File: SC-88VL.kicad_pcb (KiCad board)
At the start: 2 copper layers, 77.5 x 64.8 mm, 13 parts

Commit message: The initial design was missing a via.
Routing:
- net (no net): track 931.8 -> 931.1 mm, vias 24 -> 25

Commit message: Removed a useless via
Removed a useless via
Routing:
- net (no net): vias 25 -> 24
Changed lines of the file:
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@@
     (thickness 1.6)
     (drawings 4)
-    (tracks 176)
+    (tracks 175)
     (zones 0)
     (modules 13)
@@
   (segment (start 97.79 41.91) (end 101.6 45.72) (width 0.25) (layer B.Cu) (net 0))
   (segment (start 101.6 45.72) (end 101.6 45.72) (width 0.25) (layer B.Cu) (net 0))
-  (via (at 101.6 45.72) (size 0.8) (drill 0.4) (layers F.Cu B.Cu) (net 0))
-  (via (at 101.6 48.26) (size 0.8) (drill 0.4) (layers F.Cu B.Cu) (net 0))
+  (via (at 101.6 45.72) (size 0.8) (drill 0.4) (layers F.Cu B.Cu) (net 0) (status 1000000))
   (segment (start 101.6 45.72) (end 101.6 48.26) (width 0.25) (layer F.Cu) (net 0))
   (segment (start 102.87 59.69) (end 102.87 59.69) (width 0.25) (layer B.Cu) (net 0))

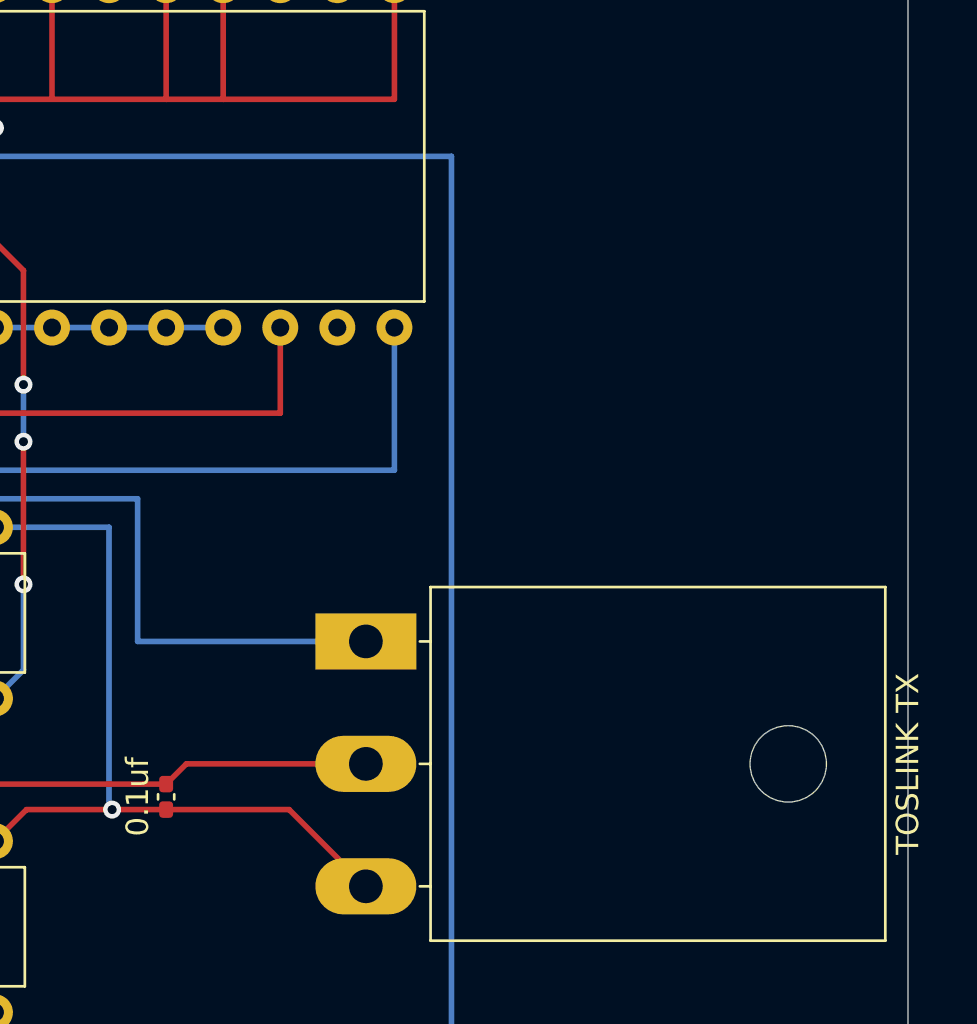
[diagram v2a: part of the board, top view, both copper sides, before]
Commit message: Added an optional TOTX170 footprint
Added an optional TOTX170 footprint, use either this one or the regular TOSLINK footprint (not both at the same time)
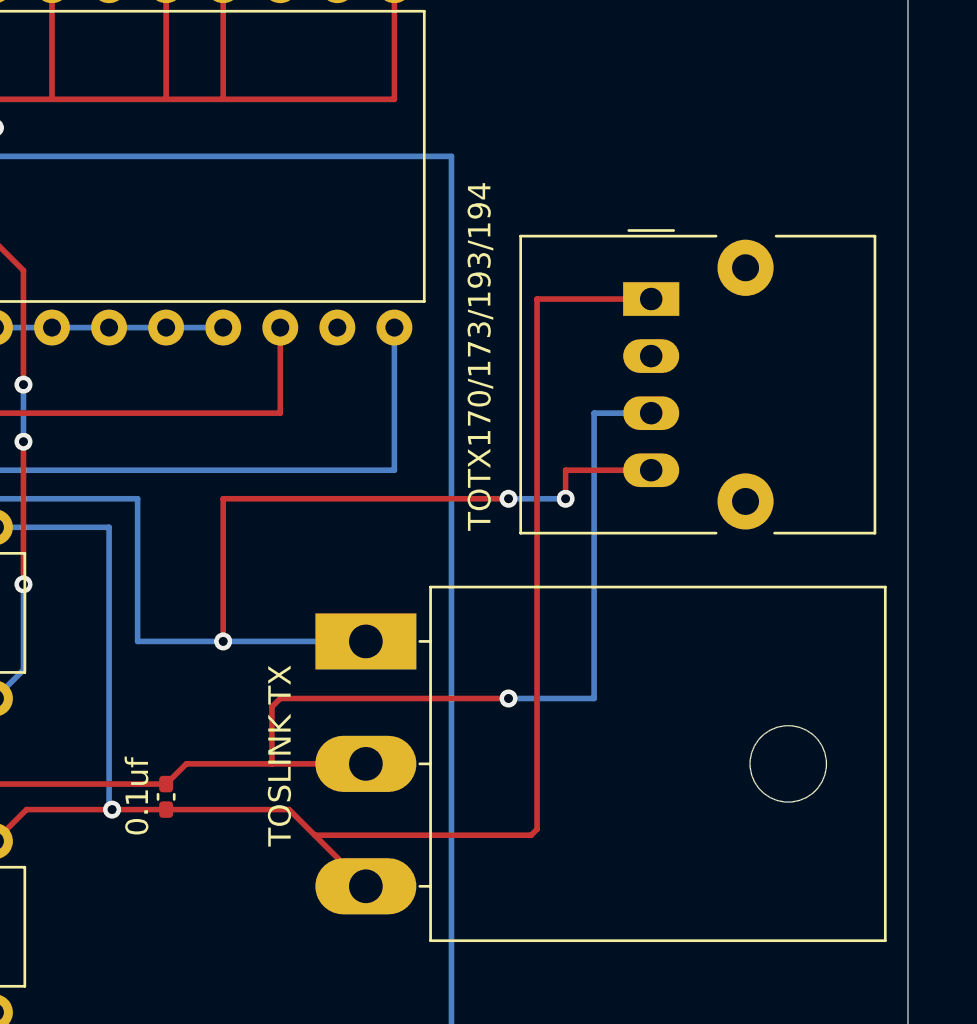
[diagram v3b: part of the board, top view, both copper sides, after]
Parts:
- added TOTX170/173/193/194: Toshiba_TOTX170_TOTX173_TOTX193_TOTX194, OptoDevice:Toshiba_TOTX170_TOTX173_TOTX193_TOTX194, F.Cu at (130.8, 53.3)
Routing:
- net (no net): track 931.1 -> 1028.7 mm, vias 24 -> 28
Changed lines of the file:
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@@
     (thickness 1.6)
     (drawings 4)
-    (tracks 175)
+    (tracks 199)
     (zones 0)
-    (modules 13)
+    (modules 14)
     (nets 1)
   )
@@
     (uvia_drill 0.1)
   )
+  (module OptoDevice:Toshiba_TOTX170_TOTX173_TOTX193_TOTX194 (layer F.Cu)
+    (at 130.81 53.34 270)
+    (descr "Fiberoptic Reciver, RX, Toshiba, Toslink, TORX170, TORX173, TORX193, TORX194")
+    (tags "Fiberoptic Reciver RX Toshiba Toslink TORX170 TORX173 TORX193 TORX194")
+    (fp_text reference TOTX170/173/193/194 (at 2.54 7.62 90) (layer F.SilkS)
+      (effects (font (size 1 1) (thickness 0.15)))
+    )
+    (fp_text value Toshiba_TOTX170_TOTX173_TOTX193_TOTX194 (at 3.81 7 90) (layer F.Fab)
+      (effects (font (size 1 1) (thickness 0.15)))
+    )
+    (fp_line (start -3.05 1) (end -3.05 -1) (layer F.SilkS) (width 0.12))
+    (fp_line (start -1.69 0) (end -2.69 -1) (layer F.Fab) (width 0.1))
+    (fp_line (start -1.69 0) (end -2.69 1) (layer F.Fab) (width 0.1))
+    (fp_line (start -2.69 -1) (end -2.69 -9.85) (layer F.Fab) (width 0.1))
+    (fp_line (start 10.56 5.95) (end -2.94 5.95) (layer F.CrtYd) (width 0.05))
+    (fp_line (start 10.56 5.95) (end 10.56 -10.1) (layer F.CrtYd) (width 0.05))
+    (fp_line (start -2.94 -10.1) (end -2.94 5.95) (layer F.CrtYd) (width 0.05))
+    (fp_line (start -2.94 -10.1) (end 10.56 -10.1) (layer F.CrtYd) (width 0.05))
+    (fp_line (start -2.8 5.81) (end 10.42 5.81) (layer F.SilkS) (width 0.12))
+    (fp_line (start 10.42 -9.96) (end -2.8 -9.96) (layer F.SilkS) (width 0.12))
+    (fp_line (start 1.81 -8.1) (end 1.81 -9.1) (layer F.Fab) (width 0.1))
+    (fp_line (start 5.81 -8.1) (end 1.81 -8.1) (layer F.Fab) (width 0.1))
+    (fp_line (start 5.81 -9.1) (end 5.81 -8.1) (layer F.Fab) (width 0.1))
+    (fp_line (start 1.81 -9.1) (end 5.81 -9.1) (layer F.Fab) (width 0.1))
+    (fp_line (start 10.42 -9.96) (end 10.42 -5.49) (layer F.SilkS) (width 0.12))
+    (fp_line (start 10.42 5.81) (end 10.42 -2.89) (layer F.SilkS) (width 0.12))
+    (fp_line (start -2.8 -9.96) (end -2.8 -5.56) (layer F.SilkS) (width 0.12))
+    (fp_line (start -2.8 5.81) (end -2.8 -2.89) (layer F.SilkS) (width 0.12))
+    (fp_line (start -2.69 5.65) (end -2.69 1) (layer F.Fab) (width 0.1))
+    (fp_line (start -2.69 -9.85) (end 10.31 -9.85) (layer F.Fab) (width 0.1))
+    (fp_line (start 10.31 5.7) (end 10.31 -9.85) (layer F.Fab) (width 0.1))
+    (fp_line (start 10.26 5.7) (end 10.31 5.7) (layer F.Fab) (width 0.1))
+    (fp_line (start -2.69 5.7) (end 10.26 5.7) (layer F.Fab) (width 0.1))
+    (fp_line (start -2.69 5.65) (end -2.69 5.7) (layer F.Fab) (width 0.1))
+    (fp_text user %R (at 3.81 -2.075 90) (layer F.Fab)
+      (effects (font (size 1 1) (thickness 0.15)))
+    )
+    (pad 1 thru_hole rect (at 0 0 270) (size 1.5 2.5) (drill 1) (layers *.Cu *.Mask))
+    (pad 2 thru_hole oval (at 2.54 0 270) (size 1.5 2.5) (drill 1) (layers *.Cu *.Mask))
+    (pad 3 thru_hole oval (at 5.08 0 270) (size 1.5 2.5) (drill 1) (layers *.Cu *.Mask))
+    (pad 4 thru_hole oval (at 7.62 0 270) (size 1.5 2.5) (drill 1) (layers *.Cu *.Mask))
+    (pad 5 thru_hole circle (at 9.01 -4.2 270) (size 2.5 2.5) (drill 1.2) (layers *.Cu *.Mask))
+    (pad 6 thru_hole circle (at -1.39 -4.2 270) (size 2.5 2.5) (drill 1.2) (layers *.Cu *.Mask))
+    (model ${KISYS3DMOD}/OptoDevice.3dshapes/Toshiba_TOTX170_TOTX173_TOTX193_TOTX194.wrl
+      (at (xyz 0 0 0))
+      (scale (xyz 1 1 1))
+      (rotate (xyz 0 0 0))
+    )
+  )
   (module Package_DIP:DIP-28_W15.24mm (layer F.Cu)
     (at 86.36 54.61 90)
@@
     (descr "TO-3P-3, Horizontal, RM 5.45mm, , see https://toshiba.semicon-storage.com/ap-en/design-support/package/detail.TO-3P(N).html")
     (tags "TO-3P-3 Horizontal RM 5.45mm ")
-    (fp_text reference "TOSLINK TX" (at 5.45 -24.12 90) (layer F.SilkS)
+    (fp_text reference "TOSLINK TX" (at 5.08 3.81 90) (layer F.SilkS)
       (effects (font (size 1 1) (thickness 0.15)))
     )
@@
     (fp_line (start -2.3 -18.8) (end -2.3 -21) (layer F.Fab) (width 0.1))
     (fp_circle (center 5.45 -18.8) (end 7.05 -18.8) (layer F.Fab) (width 0.1))
-    (fp_text user %R (at 5.45 -24.12 90) (layer F.Fab)
+    (fp_text user %R (at 5.08 3.81 90) (layer F.Fab)
       (effects (font (size 1 1) (thickness 0.15)))
     )
@@
     )
   )
+  (gr_line (start 142.24 33.02) (end 142.24 97.79) (layer Edge.Cuts) (width 0.05))
   (gr_line (start 64.77 97.79) (end 64.77 33.02) (layer Edge.Cuts) (width 0.05))
   (gr_line (start 142.24 97.79) (end 64.77 97.79) (layer Edge.Cuts) (width 0.05))
-  (gr_line (start 142.24 33.02) (end 142.24 97.79) (layer Edge.Cuts) (width 0.05))
   (gr_line (start 64.77 33.02) (end 142.24 33.02) (layer Edge.Cuts) (width 0.05))
   (segment (start 67.31 43.18) (end 67.31 35.56) (width 0.25) (layer F.Cu) (net 0))
@@
   (segment (start 78.74 62.23) (end 78.74 52.07) (width 0.25) (layer F.Cu) (net 0))
   (segment (start 78.74 52.07) (end 73.66 52.07) (width 0.25) (layer F.Cu) (net 0))
-  (segment (start 114.695 76.065) (end 118.11 79.48) (width 0.25) (layer F.Cu) (net 0))
   (segment (start 109.22 76.065) (end 114.695 76.065) (width 0.25) (layer F.Cu) (net 0))
   (segment (start 110.12 74.03) (end 109.22 74.93) (width 0.25) (layer F.Cu) (net 0))
-  (segment (start 118.11 74.03) (end 110.12 74.03) (width 0.25) (layer F.Cu) (net 0))
   (segment (start 106.815 76.065) (end 103.005 76.065) (width 0.25) (layer F.Cu) (net 0))
   (via (at 106.815 76.065) (size 0.8) (drill 0.4) (layers F.Cu B.Cu) (net 0))
@@
   (segment (start 106.68 75.93) (end 106.815 76.065) (width 0.25) (layer B.Cu) (net 0))
   (segment (start 106.68 63.5) (end 106.68 75.93) (width 0.25) (layer B.Cu) (net 0))
-  (segment (start 118.11 68.58) (end 107.95 68.58) (width 0.25) (layer B.Cu) (net 0))
+  (segment (start 118.11 68.58) (end 111.76 68.58) (width 0.25) (layer B.Cu) (net 0))
   (segment (start 107.95 68.58) (end 107.95 62.23) (width 0.25) (layer B.Cu) (net 0))
   (segment (start 107.95 62.23) (end 99.06 62.23) (width 0.25) (layer B.Cu) (net 0))
@@
   (segment (start 97.79 41.91) (end 101.6 45.72) (width 0.25) (layer B.Cu) (net 0))
   (segment (start 101.6 45.72) (end 101.6 45.72) (width 0.25) (layer B.Cu) (net 0))
-  (via (at 101.6 45.72) (size 0.8) (drill 0.4) (layers F.Cu B.Cu) (net 0) (status 1000000))
+  (via (at 101.6 45.72) (size 0.8) (drill 0.4) (layers F.Cu B.Cu) (net 0))
   (segment (start 101.6 45.72) (end 101.6 48.26) (width 0.25) (layer F.Cu) (net 0))
   (segment (start 102.87 59.69) (end 102.87 59.69) (width 0.25) (layer B.Cu) (net 0))
@@
   (via (at 102.87 57.15) (size 0.8) (drill 0.4) (layers F.Cu B.Cu) (net 0))
   (segment (start 102.87 57.15) (end 102.87 59.69) (width 0.25) (layer B.Cu) (net 0))
+  (segment (start 115.835 77.205) (end 125.465 77.205) (width 0.25) (layer F.Cu) (net 0))
+  (segment (start 114.695 76.065) (end 115.835 77.205) (width 0.25) (layer F.Cu) (net 0))
+  (segment (start 115.835 77.205) (end 118.11 79.48) (width 0.25) (layer F.Cu) (net 0))
+  (segment (start 125.465 77.205) (end 125.73 76.94) (width 0.25) (layer F.Cu) (net 0))
+  (segment (start 125.73 76.94) (end 125.73 53.34) (width 0.25) (layer F.Cu) (net 0))
+  (segment (start 125.73 53.34) (end 130.81 53.34) (width 0.25) (layer F.Cu) (net 0))
+  (segment (start 113.93 74.03) (end 113.93 71.49) (width 0.25) (layer F.Cu) (net 0))
+  (segment (start 118.11 74.03) (end 113.93 74.03) (width 0.25) (layer F.Cu) (net 0))
+  (segment (start 113.93 74.03) (end 110.12 74.03) (width 0.25) (layer F.Cu) (net 0))
+  (segment (start 113.93 71.49) (end 114.3 71.12) (width 0.25) (layer F.Cu) (net 0))
+  (segment (start 114.3 71.12) (end 124.46 71.12) (width 0.25) (layer F.Cu) (net 0))
+  (segment (start 124.46 71.12) (end 124.46 71.12) (width 0.25) (layer F.Cu) (net 0))
+  (via (at 124.46 71.12) (size 0.8) (drill 0.4) (layers F.Cu B.Cu) (net 0))
+  (segment (start 111.76 68.58) (end 107.95 68.58) (width 0.25) (layer B.Cu) (net 0))
+  (via (at 111.76 68.58) (size 0.8) (drill 0.4) (layers F.Cu B.Cu) (net 0))
+  (segment (start 111.76 68.58) (end 111.76 62.23) (width 0.25) (layer F.Cu) (net 0))
+  (segment (start 111.76 62.23) (end 124.46 62.23) (width 0.25) (layer F.Cu) (net 0))
+  (segment (start 128.27 58.42) (end 130.81 58.42) (width 0.25) (layer B.Cu) (net 0))
+  (segment (start 128.27 71.12) (end 128.27 58.42) (width 0.25) (layer B.Cu) (net 0))
+  (segment (start 124.46 71.12) (end 128.27 71.12) (width 0.25) (layer B.Cu) (net 0))
+  (via (at 127 62.23) (size 0.8) (drill 0.4) (layers F.Cu B.Cu) (net 0))
+  (segment (start 124.46 62.23) (end 124.46 62.23) (width 0.25) (layer F.Cu) (net 0))
+  (via (at 124.46 62.23) (size 0.8) (drill 0.4) (layers F.Cu B.Cu) (net 0))
+  (segment (start 124.46 62.23) (end 127 62.23) (width 0.25) (layer B.Cu) (net 0))
+  (segment (start 127 62.23) (end 127 60.96) (width 0.25) (layer F.Cu) (net 0))
+  (segment (start 127 60.96) (end 130.81 60.96) (width 0.25) (layer F.Cu) (net 0))
 )

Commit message: Added silkscreen markings
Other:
- board text added: "By Mathieulh, original schematics by UYO https://github.com/mathieulh/SC-88VL_Toslink/"
- board text added: "Revision 4"
- board text added: "SC-88/SC-88VL TOSLINK PCB"
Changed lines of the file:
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@@
   (general
     (thickness 1.6)
-    (drawings 4)
+    (drawings 7)
     (tracks 199)
     (zones 0)
@@
     )
   )
+  (gr_text "Revision 4" (at 69.85 90.17) (layer F.SilkS)
+    (effects (font (size 1 1) (thickness 0.25)))
+  )
+  (gr_text "By Mathieulh, original schematics by UYO\nhttps://github.com/mathieulh/SC-88VL_Toslink/\n" (at 78.74 93.98) (layer F.SilkS)
+    (effects (font (size 0.7 0.7) (thickness 0.125)))
+  )
+  (gr_text "SC-88/SC-88VL TOSLINK PCB" (at 77.47 87.63) (layer F.SilkS)
+    (effects (font (size 1 1) (thickness 0.25)))
+  )
   (gr_line (start 142.24 33.02) (end 142.24 97.79) (layer Edge.Cuts) (width 0.05))

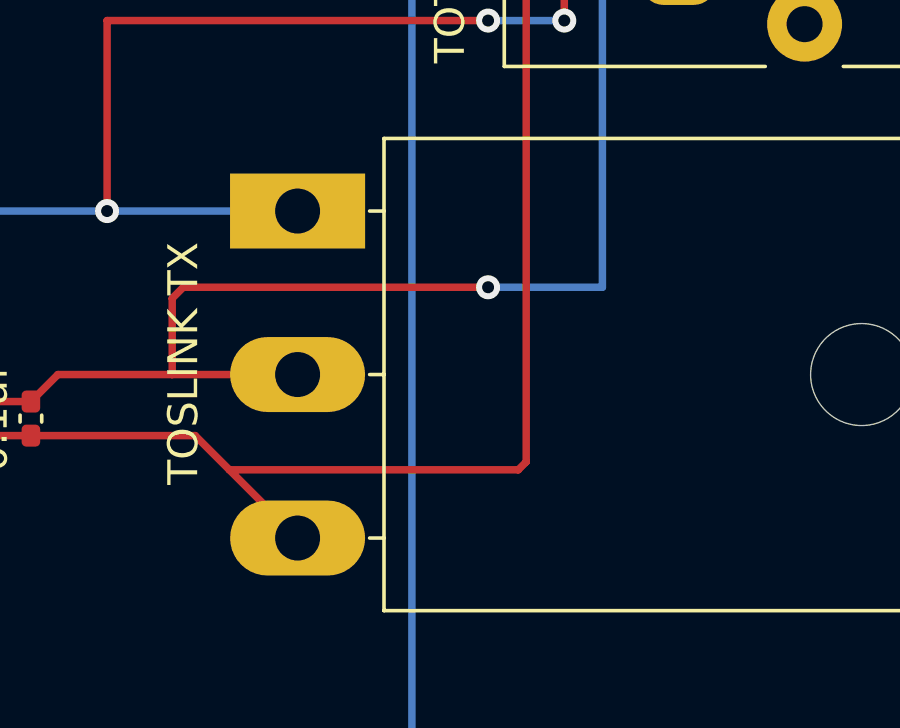
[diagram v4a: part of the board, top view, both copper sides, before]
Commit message: Added markings for deported/manual Toslink TX install
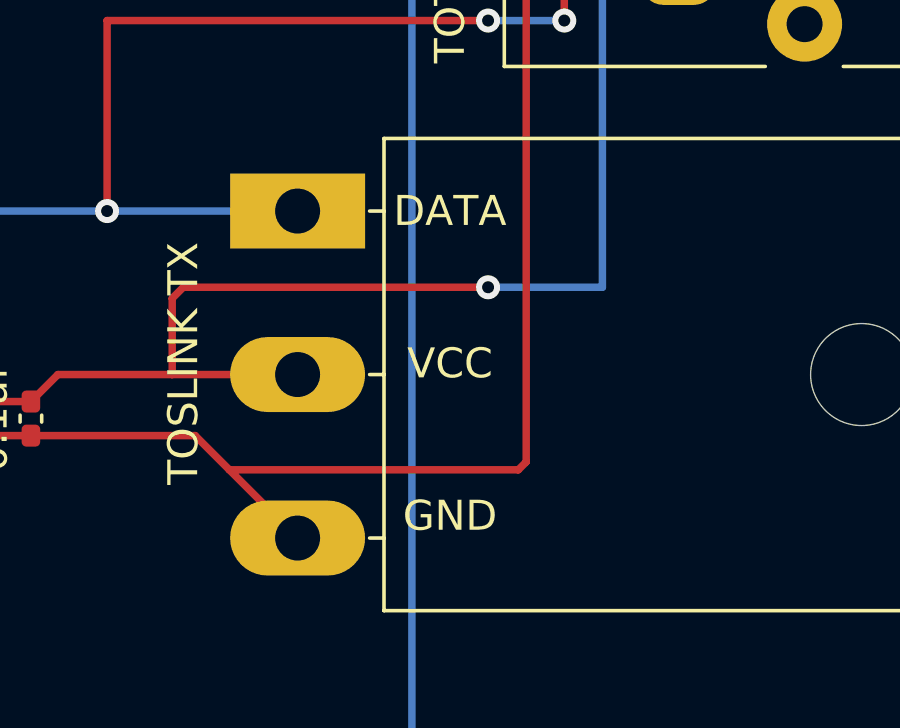
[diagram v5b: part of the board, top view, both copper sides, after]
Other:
- board text added: "DATA"
- board text added: "GND"
- board text added: "VCC"
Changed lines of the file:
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@@
   (general
     (thickness 1.6)
-    (drawings 7)
+    (drawings 10)
     (tracks 199)
     (zones 0)
@@
     )
   )
+  (gr_text GND (at 123.19 78.74) (layer F.SilkS)
+    (effects (font (size 1 1) (thickness 0.25)))
+  )
+  (gr_text VCC (at 123.19 73.66) (layer F.SilkS)
+    (effects (font (size 1 1) (thickness 0.25)))
+  )
+  (gr_text DATA (at 123.19 68.58) (layer F.SilkS)
+    (effects (font (size 1 1) (thickness 0.25)))
+  )
   (gr_text "Revision 4" (at 69.85 90.17) (layer F.SilkS)

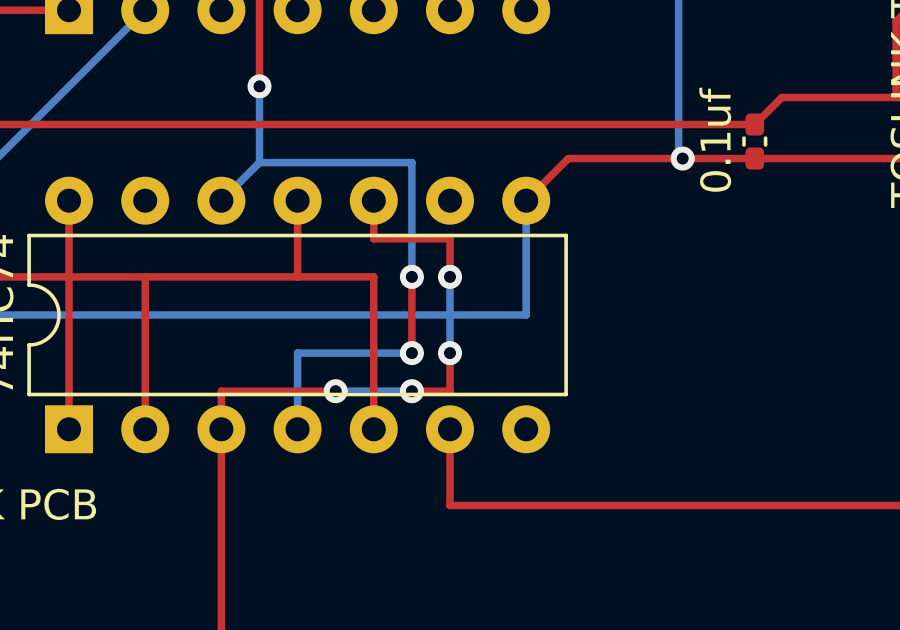
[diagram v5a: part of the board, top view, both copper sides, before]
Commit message: Fixed a short.
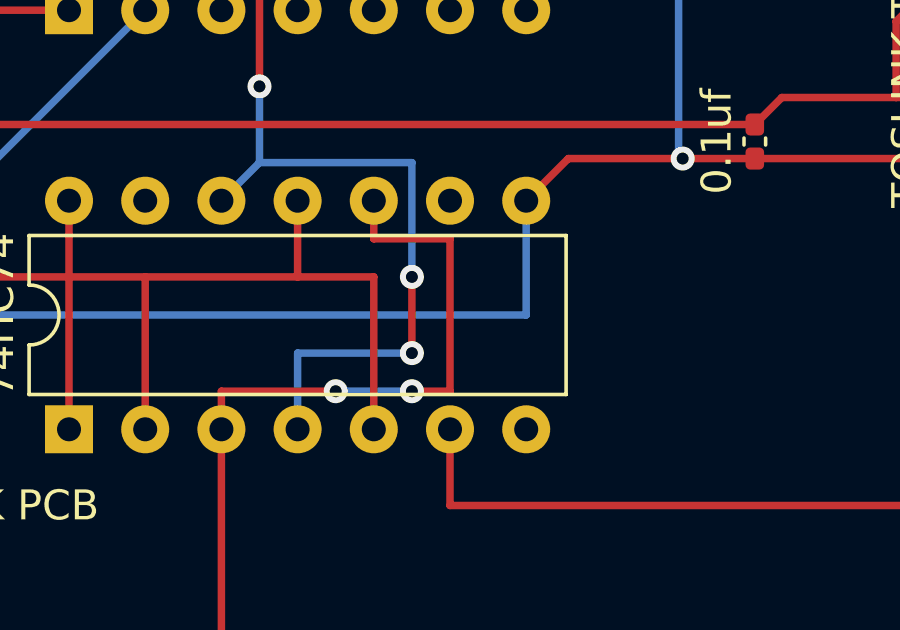
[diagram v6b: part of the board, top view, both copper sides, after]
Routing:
- net (no net): vias 28 -> 26
